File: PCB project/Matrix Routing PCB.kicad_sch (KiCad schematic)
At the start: 4 parts

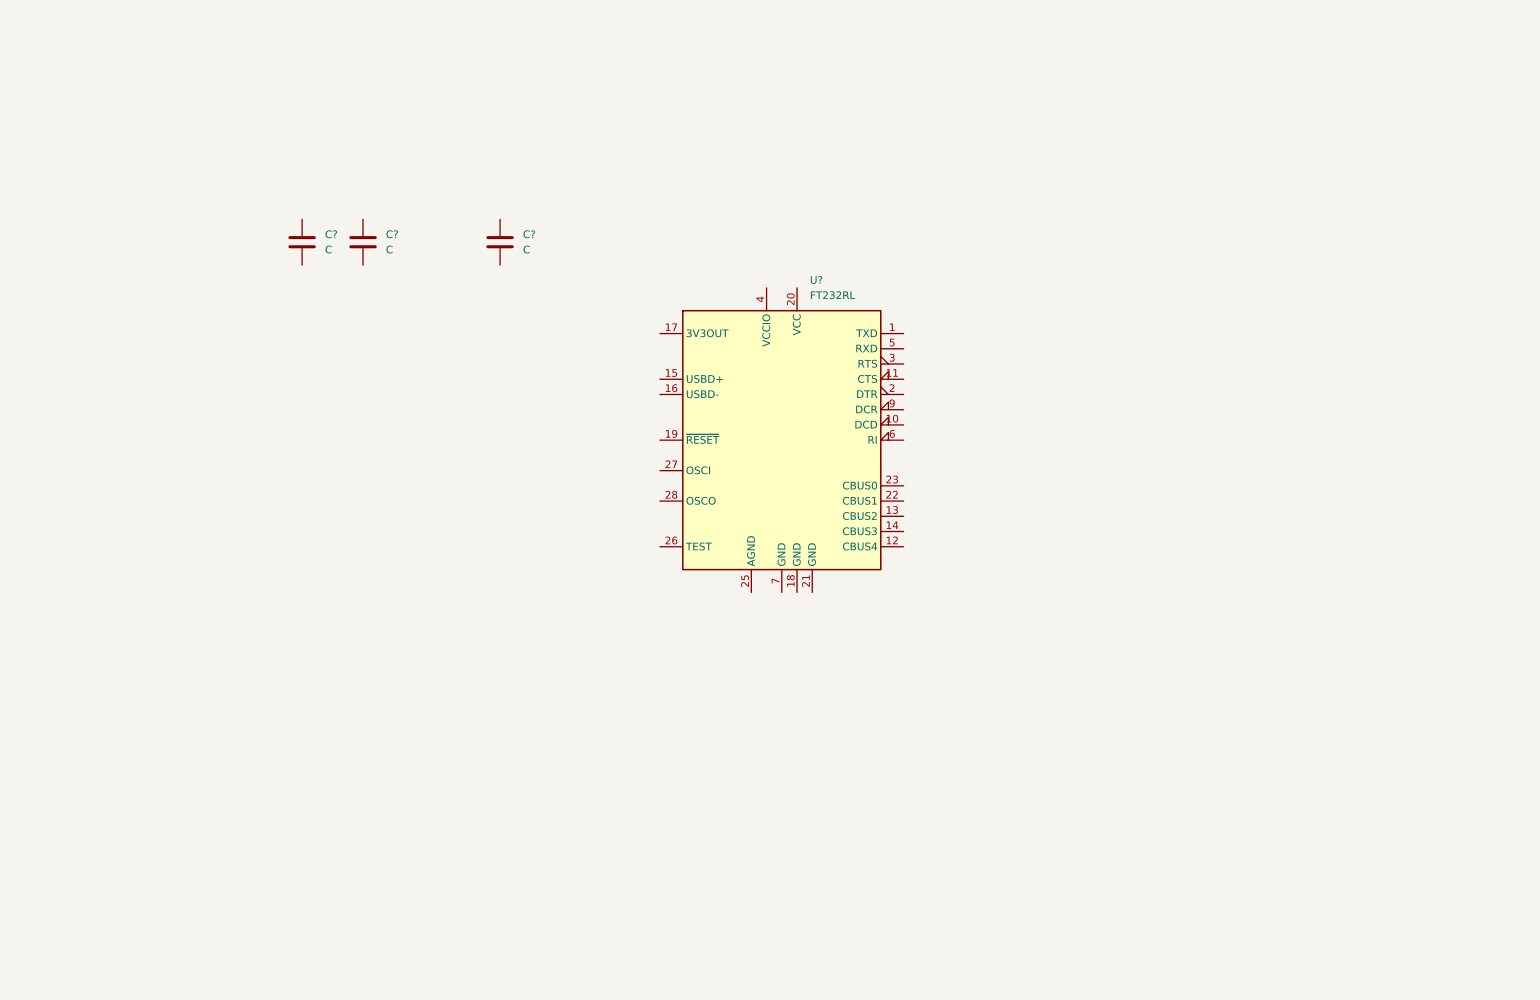
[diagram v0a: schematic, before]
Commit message: All connectors are added to the schematic with the libraries
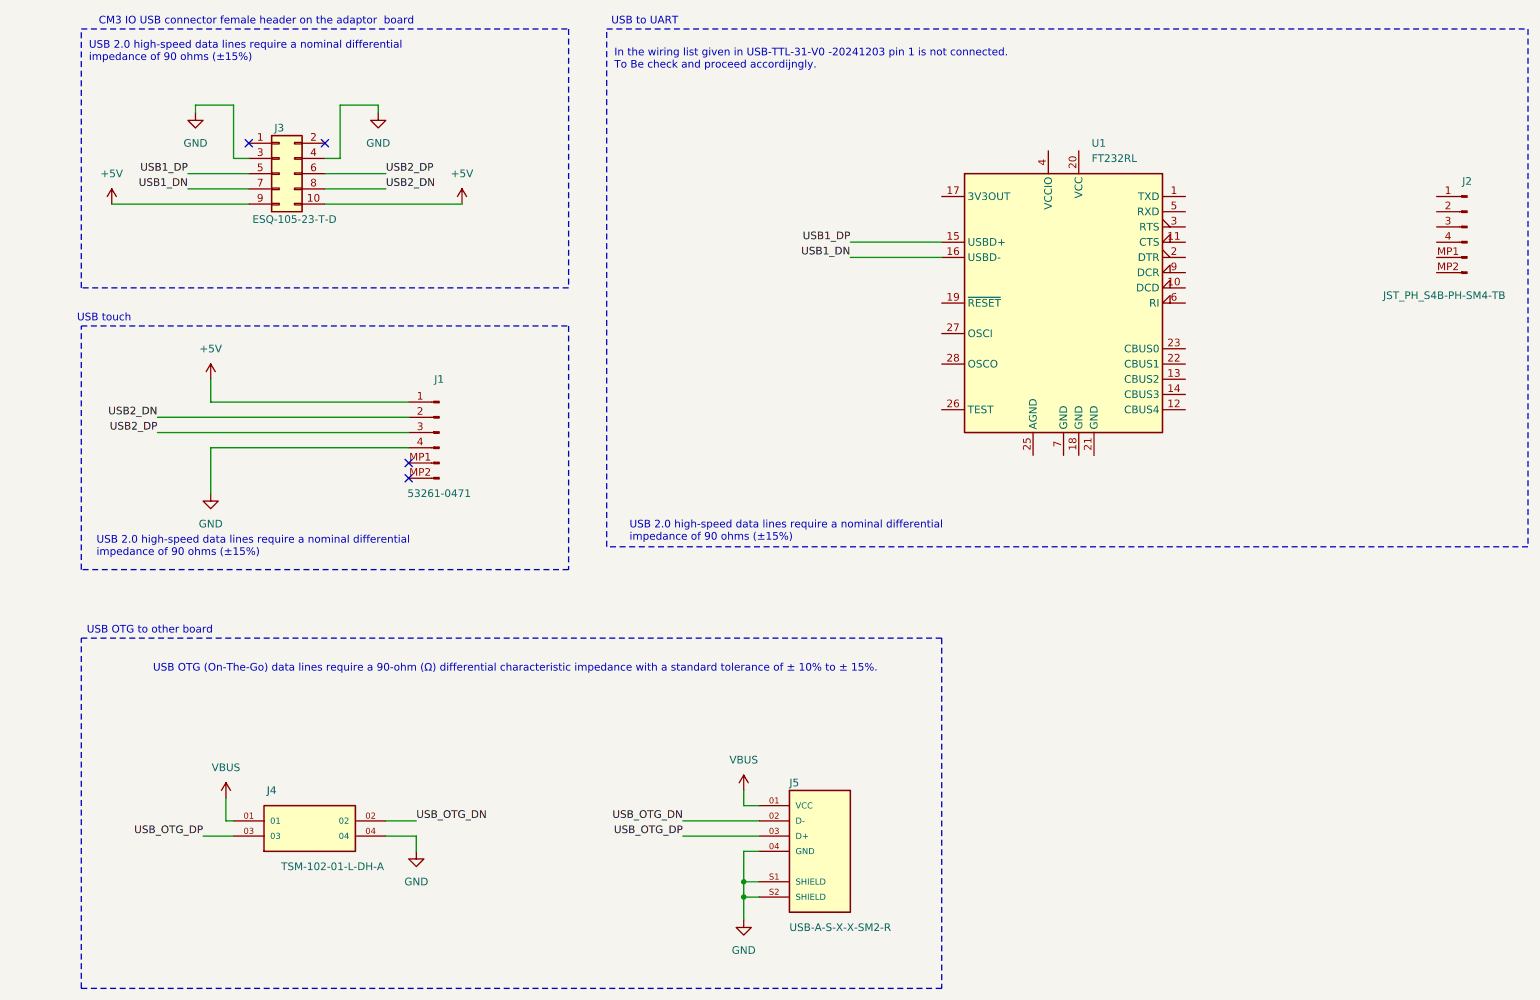
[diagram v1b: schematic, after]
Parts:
- removed C? (x2): C, symbol Device:C
- removed C?: C, Capacitor_SMD:C_0603_1608Metric_Pad1.08x0.95mm_HandSolder, symbol Device:C
- removed U?: FT232RL, Package_DFN_QFN:WDFN-12-1EP_3x3mm_P0.45mm_EP1.7x2.5mm, symbol Interface_USB:FT232RL
- added J1: 53261-0471, Matrix Routing PCB:Molex_PicoBlade_53261-0471_1x04-1MP_P1.25mm_Horizontal, symbol Matrix Routing PCB:Molex_PicoBlade_53261-0471
- added J2: JST_PH_S4B-PH-SM4-TB, Matrix Routing PCB:JST_PH_S4B-PH-SM4-TB_1x04-1MP_P2.00mm_Horizontal, symbol Matrix Routing PCB:JST_PH_S4B-PH-SM4-TB_1x04-1MP_P2.00mm_Horizontal
- added J3: ESQ-105-23-T-D, Matrix Routing PCB:ESQ-105-XX-X-D, symbol Matrix Routing PCB:Conn_02x05_Odd_Even
- added J4: TSM-102-01-L-DH-A, Matrix Routing PCB:SAMTEC_TSM-102-01-L-DH-A, symbol Matrix Routing PCB:TSM-102-01-L-DH-A
- added J5: USB-A-S-X-X-SM2-R, Matrix Routing PCB:SAMTEC_USB-A-S-X-X-SM2-R, symbol Matrix Routing PCB:USB-A-S-X-X-SM2-R
- added U1: FT232RL, Package_SO:SSOP-28_5.3x10.2mm_P0.65mm, symbol Matrix:FT232RL
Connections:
- new net +5V: J1.1 (Pin_1), J3.10 (Pin_10), J3.9 (Pin_9)
- new net GND: J1.4 (Pin_4), J3.3 (Pin_3), J3.4 (Pin_4), J4.04, J5.04 (GND), J5.S1 (SHIELD), J5.S2 (SHIELD)
- new net USB1_DN: J3.7 (Pin_7), U1.16 (USBD-)
- new net USB1_DP: J3.5 (Pin_5), U1.15 (USBD+)
- new net USB2_DN: J1.2 (Pin_2), J3.8 (Pin_8)
- new net USB2_DP: J1.3 (Pin_3), J3.6 (Pin_6)
- new net USB_OTG_DN: J4.02, J5.02 (D-)
- new net USB_OTG_DP: J4.03, J5.03 (D+)
- new net VBUS: J4.01, J5.01 (VCC)
- no-connect marks 0 -> 4
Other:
- note added: "CM3 IO USB connector female header on the adaptor board"
- note added: "In the wiring list given in USB-TTL-31-V0 -20241203 pin 1 is not connected. To Be check and proceed accordijngly."
- note added: "USB 2.0 high-speed data lines require a nominal differential impedance of 90 ohms (±15%)"
- note added: "USB OTG (On-The-Go) data lines require a 90-ohm (Ω) differential characteristic impedance with a standard tolerance of ± 10% to ± 15%."
- note added: "USB OTG to other board"
- note added: "USB to UART"
- note added: "USB touch"

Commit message: Schematic finish
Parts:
- added C?: 4.7uF, symbol Device:C
- added C? (x2): 100nF, symbol Device:C
- added C?: 10nF, symbol Device:C
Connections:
- net +5V: now also U1.20 (VCC), U1.4 (VCCIO), C?.1, C?.1, C?.1
- net GND: now also J2.4 (Pin_4), J4.03, U1.18 (GND), U1.21 (GND), U1.25 (AGND), U1.7 (GND), C?.2, C?.2, C?.2, C?.2; no longer J4.04
- net USB_OTG_DN: now also J4.04; no longer J4.02
- net USB_OTG_DP: now also J4.02; no longer J4.03
- net RX_FTDI_TX_BOARD: now reaches J2.2 (Pin_2)
- net RX_FTDI_TX_BOARD: now also U1.5 (RXD)
- net TX_FTDI_RX_BOARD: now reaches J2.3 (Pin_3)
- net TX_FTDI_RX_BOARD: now also U1.1 (TXD)
- net at U1.17 (3V3OUT): now also C?.1
- no-connect marks 4 -> 22
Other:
- note added: "Page 9 CN5 table: Serial Port Connector 1---+5V---+5V 2---TX----Serial TX 3---RX----Serial RX 4---GND---Earth wire It is assumed that TX in the table is the TX of the board and RX from FTDI needs to be connected. Please confirm. It is assumed that RX in the table is the RX of hte board and TX from FTDI needs to be connected. Please confirm."
- note added: "Please note that in the schematic pin 1 is set floating as the document of the ftdi cable said not connect. Please confirm????"
- note added: "Reference designs"
- note added: "USB OTG (On-The-Go) data lines require a 90-ohm (Ω) differential characteristic impedance with a standard tolerance of ± 10% to ± 15%. The USB OTG has a different power net not connected to the 5V from the other 2 USBs. Please confirm."
- note removed: "USB OTG (On-The-Go) data lines require a 90-ohm (Ω) differential characteristic impedance with a standard tolerance of ± 10% to ± 15%."
- title: (none) -> Matrix
- moved on the sheet: J1, J2, J3, J4, J5, U1

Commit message: House keeping changes
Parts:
- C1, C2, C3, C4: renamed from C?; footprint (none) -> Capacitor_SMD:C_0603_1608Metric

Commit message: Add the confirmation notes
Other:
- note added: "Confirmation notes: 1) J2 pin 1 is floating. 2) J2 pin 2 is TX for the connected board so FTDI RX is connected to it. 3) J2 pin 3 is RX for the connected board so FTDI TX is connected ot it. 4) USB OTG has a different VBUS power rail. The USB OTG has to work as device so ID pin needs to be left floating. Please note the ID pin is not fan out so it is floating."
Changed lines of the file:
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@@
+	)
+	(rectangle
+		(start 266.7 165.1)
+		(end 381 203.2)
+		(stroke
+			(width 0)
+			(type default)
+		)
+		(fill
+			(type none)
+		)
 	)
 	(rectangle
@@
 		)
 	)
+	(text "Confirmation notes:\n\n1) J2 pin 1 is floating.\n2) J2 pin 2 is TX for the connected board so FTDI RX is connected to it.\n3) J2 pin 3 is RX for the connected board so FTDI TX is connected ot it.\n4) USB OTG has a different VBUS power rail. The USB OTG has to\nwork as device so ID pin needs to be left floating. Please note\nthe ID pin is not fan out so it is floating."
+		(exclude_from_sim no)
+		(at 267.97 182.88 0)
+		(effects
+			(font
+				(size 2 2)
+			)
+			(justify left)
+		)
+	)

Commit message: Placement to review
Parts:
- J2: footprint Matrix Routing PCB:JST_PH_S4B-PH-SM4-TB_1x04-1MP_P2.00mm_Horizontal -> Matrix Routing PCB:S4BXHSM4TBLFSN
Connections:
- net USB1_DN: now also J1.2 (Pin_2); no longer U1.16 (USBD-)
- net USB1_DP: now also J1.3 (Pin_3); no longer U1.15 (USBD+)
- net USB2_DN: now also U1.16 (USBD-); no longer J1.2 (Pin_2)
- net USB2_DP: now also U1.15 (USBD+); no longer J1.3 (Pin_3)
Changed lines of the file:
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@@
 		)
 	)
-	(label "USB2_DN"
+	(label "USB1_DN"
 		(at 90.17 111.76 180)
 		(effects
@@
 		)
 	)
-	(label "USB2_DP"
+	(label "USB1_DP"
 		(at 90.17 114.3 180)
 		(effects
@@
 		)
 	)
-	(label "USB1_DN"
+	(label "USB2_DN"
 		(at 195.58 83.82 180)
 		(effects
@@
 		)
 	)
-	(label "USB1_DP"
+	(label "USB2_DP"
 		(at 195.58 81.28 180)
 		(effects
@@
 			)
 		)
-		(property "Footprint" "Matrix Routing PCB:JST_PH_S4B-PH-SM4-TB_1x04-1MP_P2.00mm_Horizontal"
+		(property "Footprint" "Matrix Routing PCB:S4BXHSM4TBLFSN"
 			(at 308.61 76.2 0)
 			(hide yes)

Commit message: Placement is done and 3D generated
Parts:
- added FID1, FID2, FID3: Fiducial, Fiducial:Fiducial_0.5mm_Mask1.5mm, symbol Mechanical:Fiducial
- added H1: MountingHole, MountingHole:MountingHole_3.2mm_M3, symbol Mechanical:MountingHole
- J2: footprint Matrix Routing PCB:S4BXHSM4TBLFSN -> Matrix Routing PCB:JST_PH_S4B-PH-SM4-TB_1x04-1MP_P2.00mm_Horizontal
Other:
- note added: "Mechanical"

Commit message: Make J2 and J5 part of the project library
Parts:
- C1, C3: value 100nF -> C
- C2: value 10nF -> C
- C4: value 4.7uF -> C
- J1: value 53261-0471 -> Connector 1x6
- J2: value JST_PH_S4B-PH-SM4-TB -> JST_PH_S4B-PH-SM4-TB_1x04-1MP_P2.00mm_Horizontal
- J3: value ESQ-105-23-T-D -> ESQ-105-11-T-D
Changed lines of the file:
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@@
 			)
 		)
-		(property "Value" "4.7uF"
+		(property "Value" "C"
 			(at 257.81 59.6899 0)
 			(show_name no)
@@
 		(dnp no)
 		(fields_autoplaced yes)
-		(property "Reference" "#PWR01"
+		(property "Reference" "#PWR1"
 			(at 127 67.31 0)
 			(hide yes)
@@
 			(project "Matrix Routing PCB"
 				(path "/185b37f5-114c-43cd-be29-6d66c089f841"
-					(reference "#PWR01")
+					(reference "#PWR1")
 					(unit 1)
 				)
@@
 		(dnp no)
 		(fields_autoplaced yes)
-		(property "Reference" "#FLG03"
+		(property "Reference" "#FLG3"
 			(at 96.52 57.785 0)
 			(hide yes)
@@
 			(project "Matrix Routing PCB"
 				(path "/185b37f5-114c-43cd-be29-6d66c089f841"
-					(reference "#FLG03")
+					(reference "#FLG3")
 					(unit 1)
 				)
@@
 			)
 		)
-		(property "Value" "100nF"
+		(property "Value" "C"
 			(at 168.91 82.55 0)
 			(show_name no)
@@
 		(dnp no)
 		(fields_autoplaced yes)
-		(property "Reference" "#FLG02"
+		(property "Reference" "#FLG2"
 			(at 98.425 200.66 0)
 			(hide yes)
@@
 			(project "Matrix Routing PCB"
 				(path "/185b37f5-114c-43cd-be29-6d66c089f841"
-					(reference "#FLG02")
+					(reference "#FLG2")
 					(unit 1)
 				)
@@
 		(dnp no)
 		(fields_autoplaced yes)
-		(property "Reference" "#PWR017"
+		(property "Reference" "#PWR17"
 			(at 228.6 58.42 0)
 			(hide yes)
@@
 			(project "Matrix Routing PCB"
 				(path "/185b37f5-114c-43cd-be29-6d66c089f841"
-					(reference "#PWR017")
+					(reference "#PWR17")
 					(unit 1)
 				)
@@
 		(dnp no)
 		(fields_autoplaced yes)
-		(property "Reference" "#PWR08"
+		(property "Reference" "#PWR8"
 			(at 100.33 213.36 0)
 			(hide yes)
@@
 			(project "Matrix Routing PCB"
 				(path "/185b37f5-114c-43cd-be29-6d66c089f841"
-					(reference "#PWR08")
+					(reference "#PWR8")
 					(unit 1)
 				)
@@
 		(dnp no)
 		(fields_autoplaced yes)
-		(property "Reference" "#PWR010"
+		(property "Reference" "#PWR10"
 			(at 186.69 199.39 0)
 			(hide yes)
@@
 			(project "Matrix Routing PCB"
 				(path "/185b37f5-114c-43cd-be29-6d66c089f841"
-					(reference "#PWR010")
+					(reference "#PWR10")
 					(unit 1)
 				)
@@
 			)
 		)
-		(property "Value" "JST_PH_S4B-PH-SM4-TB"
+		(property "Value" "JST_PH_S4B-PH-SM4-TB_1x04-1MP_P2.00mm_Horizontal"
 			(at 304.8 87.63 0)
 			(show_name no)
@@
 		(dnp no)
 		(fields_autoplaced yes)
-		(property "Reference" "#PWR03"
+		(property "Reference" "#PWR3"
 			(at 99.06 130.81 0)
 			(hide yes)
@@
 			(project "Matrix Routing PCB"
 				(path "/185b37f5-114c-43cd-be29-6d66c089f841"
-					(reference "#PWR03")
+					(reference "#PWR3")
 					(unit 1)
 				)
@@
 		(dnp no)
 		(fields_autoplaced yes)
-		(property "Reference" "#PWR011"
+		(property "Reference" "#PWR11"
 			(at 290.83 97.79 0)
 			(hide yes)
@@
 			(project "Matrix Routing PCB"
 				(path "/185b37f5-114c-43cd-be29-6d66c089f841"
-					(reference "#PWR011")
+					(reference "#PWR11")
 					(unit 1)
 				)
@@
 		(dnp no)
 		(fields_autoplaced yes)
-		(property "Reference" "#PWR07"
+		(property "Reference" "#PWR7"
 			(at 186.69 223.52 0)
 			(hide yes)
@@
 			(project "Matrix Routing PCB"
 				(path "/185b37f5-114c-43cd-be29-6d66c089f841"
-					(reference "#PWR07")
+					(reference "#PWR7")
 					(unit 1)
 				)
@@
 		(dnp no)
 		(fields_autoplaced yes)
-		(property "Reference" "#PWR015"
+		(property "Reference" "#PWR15"
 			(at 226.06 127 0)
 			(hide yes)
@@
 			(project "Matrix Routing PCB"
 				(path "/185b37f5-114c-43cd-be29-6d66c089f841"
-					(reference "#PWR015")
+					(reference "#PWR15")
 					(unit 1)
 				)
@@
 			)
 		)
-		(property "Value" "ESQ-105-23-T-D"
+		(property "Value" "ESQ-105-11-T-D"
 			(at 113.03 78.74 0)
 			(show_name no)
@@
 		(dnp no)
 		(fields_autoplaced yes)
-		(property "Reference" "#PWR013"
+		(property "Reference" "#PWR13"
 			(at 241.3 68.58 0)
 			(hide yes)
@@
 			(project "Matrix Routing PCB"
 				(path "/185b37f5-114c-43cd-be29-6d66c089f841"
-					(reference "#PWR013")
+					(reference "#PWR13")
 					(unit 1)
 				)
@@
 			)
 		)
-		(property "Value" "53261-0471"
+		(property "Value" "Connector 1x6"
 			(at 137.16 124.46 0)
 			(show_name no)
@@
 		(dnp no)
 		(fields_autoplaced yes)
-		(property "Reference" "#PWR04"
+		(property "Reference" "#PWR4"
 			(at 140.97 80.01 0)
 			(hide yes)
@@
 			(project "Matrix Routing PCB"
 				(path "/185b37f5-114c-43cd-be29-6d66c089f841"
-					(reference "#PWR04")
+					(reference "#PWR4")
 					(unit 1)
 				)
@@
 			)
 		)
-		(property "Value" "10nF"
+		(property "Value" "C"
 			(at 215.9 60.9599 0)
 			(show_name no)
@@
 		(dnp no)
 		(fields_autoplaced yes)
-		(property "Reference" "#PWR016"
+		(property "Reference" "#PWR16"
 			(at 177.8 91.44 0)
 			(hide yes)
@@
 			(project "Matrix Routing PCB"
 				(path "/185b37f5-114c-43cd-be29-6d66c089f841"
-					(reference "#PWR016")
+					(reference "#PWR16")
 					(unit 1)
 				)
@@
 			)
 		)
-		(property "Value" "100nF"
+		(property "Value" "C"
 			(at 245.11 59.6899 0)
 			(show_name no)
@@
 		(dnp no)
 		(fields_autoplaced yes)
-		(property "Reference" "#PWR02"
+		(property "Reference" "#PWR2"
 			(at 96.52 67.31 0)
 			(hide yes)
@@
 			(project "Matrix Routing PCB"
 				(path "/185b37f5-114c-43cd-be29-6d66c089f841"
-					(reference "#PWR02")
+					(reference "#PWR2")
 					(unit 1)
 				)
@@
 		(dnp no)
 		(fields_autoplaced yes)
-		(property "Reference" "#PWR06"
+		(property "Reference" "#PWR6"
 			(at 99.06 109.22 0)
 			(hide yes)
@@
 			(project "Matrix Routing PCB"
 				(path "/185b37f5-114c-43cd-be29-6d66c089f841"
-					(reference "#PWR06")
+					(reference "#PWR6")
 					(unit 1)
 				)
@@
 		(dnp no)
 		(fields_autoplaced yes)
-		(property "Reference" "#FLG01"
+		(property "Reference" "#FLG1"
 			(at 111.76 107.315 0)
 			(hide yes)
@@
 			(project "Matrix Routing PCB"
 				(path "/185b37f5-114c-43cd-be29-6d66c089f841"
-					(reference "#FLG01")
+					(reference "#FLG1")
 					(unit 1)
 				)
@@
 		(dnp no)
 		(fields_autoplaced yes)
-		(property "Reference" "#PWR05"
+		(property "Reference" "#PWR5"
 			(at 82.55 80.01 0)
 			(hide yes)
@@
 			(project "Matrix Routing PCB"
 				(path "/185b37f5-114c-43cd-be29-6d66c089f841"
-					(reference "#PWR05")
+					(reference "#PWR5")
 					(unit 1)
 				)
@@
 		(dnp no)
 		(fields_autoplaced yes)
-		(property "Reference" "#PWR09"
+		(property "Reference" "#PWR9"
 			(at 100.33 200.66 0)
 			(hide yes)
@@
 			(project "Matrix Routing PCB"
 				(path "/185b37f5-114c-43cd-be29-6d66c089f841"
-					(reference "#PWR09")
+					(reference "#PWR9")
 					(unit 1)
 				)
@@
 		(dnp no)
 		(fields_autoplaced yes)
-		(property "Reference" "#PWR012"
+		(property "Reference" "#PWR12"
 			(at 212.09 69.85 0)
 			(hide yes)
@@
 			(project "Matrix Routing PCB"
 				(path "/185b37f5-114c-43cd-be29-6d66c089f841"
-					(reference "#PWR012")
+					(reference "#PWR12")
 					(unit 1)
 				)
@@
 		(dnp no)
 		(fields_autoplaced yes)
-		(property "Reference" "#PWR014"
+		(property "Reference" "#PWR14"
 			(at 254 68.58 0)
 			(hide yes)
@@
 			(project "Matrix Routing PCB"
 				(path "/185b37f5-114c-43cd-be29-6d66c089f841"
-					(reference "#PWR014")
+					(reference "#PWR14")
 					(unit 1)
 				)
